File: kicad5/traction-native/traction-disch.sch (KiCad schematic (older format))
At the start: 35 parts

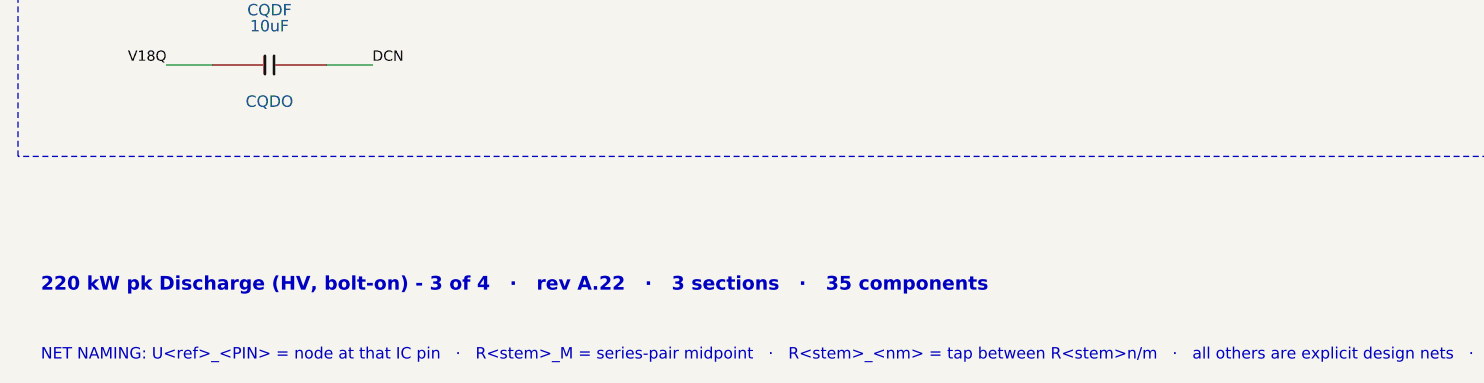
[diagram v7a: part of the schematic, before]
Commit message: Rev A.23: round 24 — four rechecks of 4ed0101 (F240–F244): the SDADC reference on its supply node, acquisition freshness, the map's flux slope and the ripple limiter's exact bounds, the temperature latch, the V_DC expiry
Hardware (F240, no new part): the S32K39 data sheet's SDADC table (Rev. 3 Table 38, in our archive and our own
extracted-parameters file) requires VREFP within ±25 mV of AVDD; the round-23 disposition had judged the general +100 mV
note and called the figure absent while the references sat on the FS26 VREF, matched to the SDADC-supply LDO only within
±1 %. Every non-R2R reference group (E6/H6 SAR, E10/F13 SDADC) is now on V5A itself with VDDA_SDADC and VDD_HV_A (NXP's
GEN3 arrangement); the ratiometric loads (HW_ID and offset dividers, the seven NTC pull-ups) moved with the reference; the
R2R ladder keeps the FS26 VREF as its isolated supply through the 10 Ω branch (CR2R1 330 nF, 37 kHz); CSB5 2.2 µF holds
the FS26 window alone (1.36–2.92 µF effective); the absolute SAR scale re-budgeted at the LDO2's ±1.75 %; ERC locks, pin
freeze, manifest, handoff §4.11 island rule (≤ 20 mΩ from E12 to any VREFH ball), VR-34 closed by design, IR-26, QP-TH-06.
Pipeline at A.23: ERC 981/0/0, verify 158/18/0, sim 23/6/0, Marine 87/23/0, 21 pages / 2065 pins, KiCad proof PASS, PDFs
and BOMs regenerated (₹72,983 unchanged). The handoff §6 gives every open pre-layout decision a provisional default.

Firmware (TI_FW_ID 0x0A0F0016, CAL layout 4, 191 fields / 92 CAL rows, 82 DTCs): F241 a stopped slow ADC channel stayed
valid forever (the caller discarded the acquisition stamp) → a three-state contract new/held/expired for every slow-list
input with cal_temp_hold_ms and DTC_ADC_SLOW_STALE, every slow consumer audited (V5GD/VOFS, IGN, INTRLOK_N, VSUP, HW_ID);
F242 the inductance map must keep a positive flux slope (≥ 0.25 × L0 below every breakpoint) and the ripple limiter bounds
every piece of its interval in closed form (breakpoints alone shown insufficient by a 20 000-m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
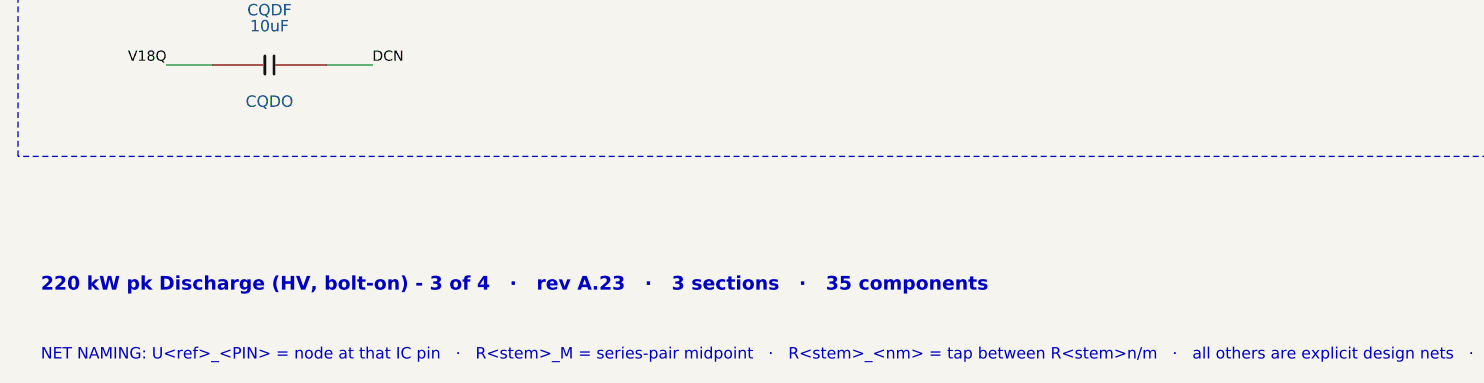
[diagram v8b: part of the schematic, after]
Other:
- note added: "220 kW pk Discharge (HV, bolt-on) - 3 of 4 · rev A.23 · 3 sections · 35 components"
- note removed: "220 kW pk Discharge (HV, bolt-on) - 3 of 4 · rev A.22 · 3 sections · 35 components"
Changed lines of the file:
@@
 Title "Traction Inverter — Discharge board (bolt-on, XM3 pattern)"
 Date "2026-09-23"
-Rev "A.22"
+Rev "A.23"
 Comp "Traction Inverter 220 kW pk - Discharge (HV, bolt-on), sheet 3 of 4"
 Comment1 "Inverter = Power board + Cap bank busbar + bolt-on Discharge board (all HV) + Control card (LV); safe state holds with any link lost"
@@
 $EndDescr
 Text Notes 600 7600 0    60   ~ 12
-220 kW pk Discharge (HV, bolt-on) - 3 of 4   ·   rev A.22   ·   3 sections   ·   35 components
+220 kW pk Discharge (HV, bolt-on) - 3 of 4   ·   rev A.23   ·   3 sections   ·   35 components
 Text Notes 600 7900 0    50   ~ 0
 NET NAMING: U<ref>_<PIN> = node at that IC pin   ·   R<stem>_M = series-pair midpoint   ·   R<stem>_<nm> = tap between R<stem>n/m   ·   all others are explicit design nets   ·   same name on another sheet = same net, joined only at the named connector/stud/tab
